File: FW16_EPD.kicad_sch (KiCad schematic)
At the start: 62 parts, among them J1 Conn_01x02, J2 Framework Input Module Connec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, J3 FH34SRJ-24S-0.5SH, J4 FH34SRJ-6S-0.5SH, Q1 DMG3404L, Q2 SSM3J338R, U1 RP2040, U2 W25Q128JVP, U3 MCP9808_DFN, Y1 12.000 MHz ABM8-272-T3

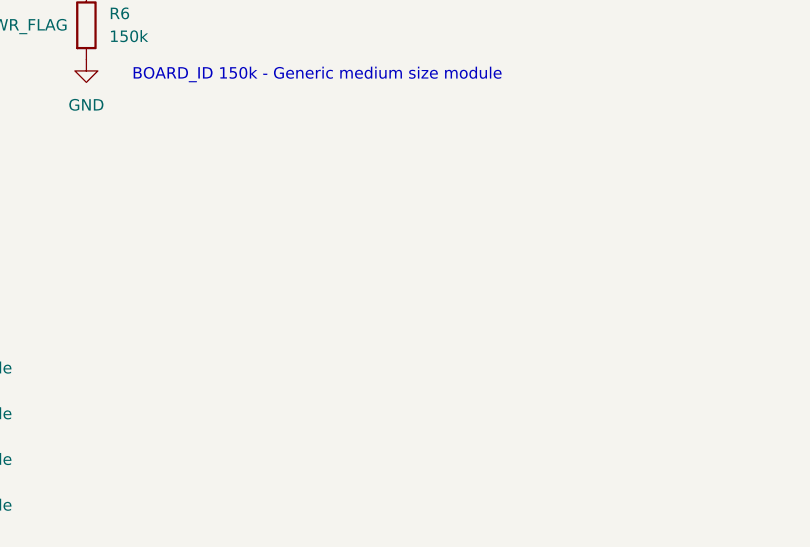
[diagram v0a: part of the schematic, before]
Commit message: sch/pcb: add TVS diodes; thicker traces for EPD DC/DC
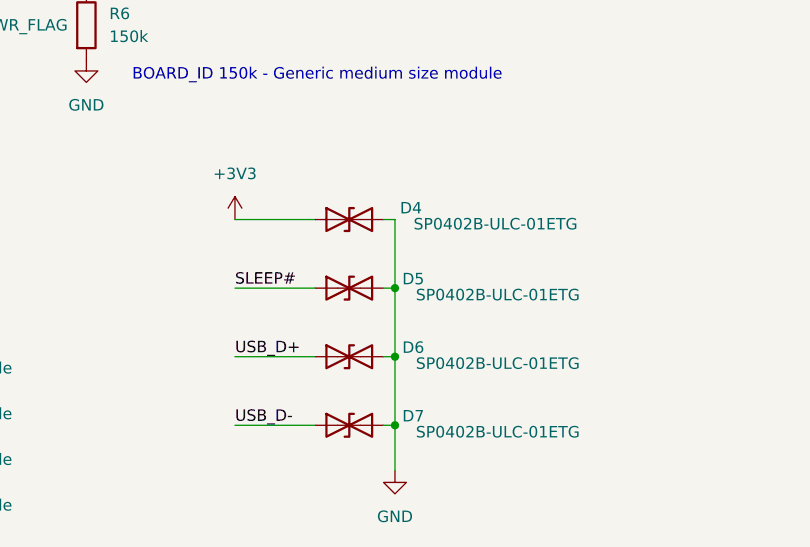
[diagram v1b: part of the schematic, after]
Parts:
- added D4, D5, D6, D7: SP0402B-ULC-01ETG, Diode_SMD:D_0402_1005Metric, symbol Device:D_TVS
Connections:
- net +3V3: now also D4.1 (A1)
- net GND: now also D4.2 (A2), D5.2 (A2), D6.2 (A2), D7.2 (A2)
- net SLEEP#: now also D5.1 (A1)
- net USB_D+: now also D6.1 (A1)
- net USB_D-: now also D7.1 (A1)

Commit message: finishing touches
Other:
- title: (none) -> Framework 16 Touchscreen EPD Module
- moved on the sheet: H1, H2, H3, H4, H5, H6, H7, H8
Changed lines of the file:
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@@
 	(generator_version "8.0")
 	(paper "A3")
+	(title_block
+		(title "Framework 16 Touchscreen EPD Module")
+		(date "2024-10-03")
+		(rev "1.0")
+	)
 	(junction
 		(at 321.31 185.42)
@@
 	(text "Magnet Holes"
 		(exclude_from_sim no)
-		(at 55.118 256.032 0)
+		(at 41.148 261.112 0)
 		(effects
 			(font
@@
 	(text "Alignment Holes"
 		(exclude_from_sim no)
-		(at 25.4 256.286 0)
+		(at 21.59 261.366 0)
 		(effects
 			(font
@@
 	(symbol
 		(lib_id "Mechanical:MountingHole")
-		(at 20.32 260.35 0)
+		(at 16.51 265.43 0)
 		(unit 1)
 		(exclude_from_sim yes)
@@
 		(fields_autoplaced yes)
 		(property "Reference" "H1"
-			(at 22.86 259.0799 0)
+			(at 19.05 264.1599 0)
 			(effects
 				(font
@@
 		)
 		(property "Value" "MountingHole"
-			(at 22.86 261.6199 0)
+			(at 19.05 266.6999 0)
 			(effects
 				(font
@@
 		)
 		(property "Footprint" "MountingHole:MountingHole_2.1mm"
-			(at 20.32 260.35 0)
+			(at 16.51 265.43 0)
 			(effects
 				(font
@@
 		)
 		(property "Datasheet" "~"
-			(at 20.32 260.35 0)
+			(at 16.51 265.43 0)
 			(effects
 				(font
@@
 		)
 		(property "Description" "Mounting Hole without connection"
-			(at 20.32 260.35 0)
+			(at 16.51 265.43 0)
 			(effects
 				(font
@@
 	(symbol
 		(lib_id "Mechanical:MountingHole")
-		(at 50.8 275.59 0)
+		(at 36.83 280.67 0)
 		(unit 1)
 		(exclude_from_sim yes)
@@
 		(fields_autoplaced yes)
 		(property "Reference" "H8"
-			(at 53.34 274.3199 0)
+			(at 39.37 279.3999 0)
 			(effects
 				(font
@@
 		)
 		(property "Value" "MountingHole"
-			(at 53.34 276.8599 0)
+			(at 39.37 281.9399 0)
 			(effects
 				(font
@@
 		)
 		(property "Footprint" "InputModule:MountingHole_3.7mm_Pad_24929"
-			(at 50.8 275.59 0)
+			(at 36.83 280.67 0)
 			(effects
 				(font
@@
 		)
 		(property "Datasheet" "~"
-			(at 50.8 275.59 0)
+			(at 36.83 280.67 0)
 			(effects
 				(font
@@
 		)
 		(property "Description" "Mounting Hole without connection"
-			(at 50.8 275.59 0)
+			(at 36.83 280.67 0)
 			(effects
 				(font
@@
 	(symbol
 		(lib_id "Mechanical:MountingHole")
-		(at 20.32 265.43 0)
+		(at 16.51 270.51 0)
 		(unit 1)
 		(exclude_from_sim yes)
@@
 		(fields_autoplaced yes)
 		(property "Reference" "H2"
-			(at 22.86 264.1599 0)
+			(at 19.05 269.2399 0)
 			(effects
 				(font
@@
 		)
 		(property "Value" "MountingHole"
-			(at 22.86 266.6999 0)
+			(at 19.05 271.7799 0)
 			(effects
 				(font
@@
 		)
 		(property "Footprint" "MountingHole:MountingHole_2.1mm"
-			(at 20.32 265.43 0)
+			(at 16.51 270.51 0)
 			(effects
 				(font
@@
 		)
 		(property "Datasheet" "~"
-			(at 20.32 265.43 0)
+			(at 16.51 270.51 0)
 			(effects
 				(font
@@
 		)
 		(property "Description" "Mounting Hole without connection"
-			(at 20.32 265.43 0)
+			(at 16.51 270.51 0)
 			(effects
 				(font
@@
 	(symbol
 		(lib_id "Mechanical:MountingHole")
-		(at 20.32 275.59 0)
+		(at 16.51 280.67 0)
 		(unit 1)
 		(exclude_from_sim yes)
@@
 		(fields_autoplaced yes)
 		(property "Reference" "H4"
-			(at 22.86 274.3199 0)
+			(at 19.05 279.3999 0)
 			(effects
 				(font
@@
 		)
 		(property "Value" "MountingHole"
-			(at 22.86 276.8599 0)
+			(at 19.05 281.9399 0)
 			(effects
 				(font
@@
 		)
 		(property "Footprint" "MountingHole:MountingHole_2.1mm"
-			(at 20.32 275.59 0)
+			(at 16.51 280.67 0)
 			(effects
 				(font
@@
 		)
 		(property "Datasheet" "~"
-			(at 20.32 275.59 0)
+			(at 16.51 280.67 0)
 			(effects
 				(font
@@
 		)
 		(property "Description" "Mounting Hole without connection"
-			(at 20.32 275.59 0)
+			(at 16.51 280.67 0)
 			(effects
 				(font
@@
 	(symbol
 		(lib_id "Mechanical:MountingHole")
-		(at 50.8 270.51 0)
+		(at 36.83 275.59 0)
 		(unit 1)
 		(exclude_from_sim yes)
@@
 		(fields_autoplaced yes)
 		(property "Reference" "H7"
-			(at 53.34 269.2399 0)
+			(at 39.37 274.3199 0)
 			(effects
 				(font
@@
 		)
 		(property "Value" "MountingHole"
-			(at 53.34 271.7799 0)
+			(at 39.37 276.8599 0)
 			(effects
 				(font
@@
 		)
 		(property "Footprint" "InputModule:MountingHole_3.7mm_Pad_24929"
-			(at 50.8 270.51 0)
+			(at 36.83 275.59 0)
 			(effects
 				(font
@@
 		)
 		(property "Datasheet" "~"
-			(at 50.8 270.51 0)
+			(at 36.83 275.59 0)
 			(effects
 				(font
@@
 		)
 		(property "Description" "Mounting Hole without connection"
-			(at 50.8 270.51 0)
+			(at 36.83 275.59 0)
 			(effects
 				(font
@@
 	(symbol
 		(lib_id "Mechanical:MountingHole")
-		(at 50.8 265.43 0)
+		(at 36.83 270.51 0)
 		(unit 1)
 		(exclude_from_sim yes)
@@
 		(fields_autoplaced yes)
 		(property "Reference" "H6"
-			(at 53.34 264.1599 0)
+			(at 39.37 269.2399 0)
 			(effects
 				(font
@@
 		)
 		(property "Value" "MountingHole"
-			(at 53.34 266.6999 0)
+			(at 39.37 271.7799 0)
 			(effects
 				(font
@@
 		)
 		(property "Footprint" "InputModule:MountingHole_3.7mm_Pad_24929"
-			(at 50.8 265.43 0)
+			(at 36.83 270.51 0)
 			(effects
 				(font
@@
 		)
 		(property "Datasheet" "~"
-			(at 50.8 265.43 0)
+			(at 36.83 270.51 0)
 			(effects
 				(font
@@
 		)
 		(property "Description" "Mounting Hole without connection"
-			(at 50.8 265.43 0)
+			(at 36.83 270.51 0)
 			(effects
 				(font
@@
 	(symbol
 		(lib_id "Mechanical:MountingHole")
-		(at 20.32 270.51 0)
+		(at 16.51 275.59 0)
 		(unit 1)
 		(exclude_from_sim yes)
@@
 		(fields_autoplaced yes)
 		(property "Reference" "H3"
-			(at 22.86 269.2399 0)
+			(at 19.05 274.3199 0)
 			(effects
 				(font
@@
 		)
 		(property "Value" "MountingHole"
-			(at 22.86 271.7799 0)
+			(at 19.05 276.8599 0)
 			(effects
 				(font
@@
 		)
 		(property "Footprint" "MountingHole:MountingHole_2.1mm"
-			(at 20.32 270.51 0)
+			(at 16.51 275.59 0)
 			(effects
 				(font
@@
 		)
 		(property "Datasheet" "~"
-			(at 20.32 270.51 0)
+			(at 16.51 275.59 0)
 			(effects
 				(font
@@
 		)
 		(property "Description" "Mounting Hole without connection"
-			(at 20.32 270.51 0)
+			(at 16.51 275.59 0)
 			(effects
 				(font
@@
 	(symbol
 		(lib_id "Mechanical:MountingHole")
-		(at 50.8 260.35 0)
+		(at 36.83 265.43 0)
 		(unit 1)
 		(exclude_from_sim yes)
@@
 		(fields_autoplaced yes)
 		(property "Reference" "H5"
-			(at 53.34 259.0799 0)
+			(at 39.37 264.1599 0)
 			(effects
 				(font
@@
 		)
 		(property "Value" "MountingHole"
-			(at 53.34 261.6199 0)
+			(at 39.37 266.6999 0)
 			(effects
 				(font
@@
 		)
 		(property "Footprint" "InputModule:MountingHole_3.7mm_Pad_24929"
-			(at 50.8 260.35 0)
+			(at 36.83 265.43 0)
 			(effects
 				(font
@@
 		)
 		(property "Datasheet" "~"
-			(at 50.8 260.35 0)
+			(at 36.83 265.43 0)
 			(effects
 				(font
@@
 		)
 		(property "Description" "Mounting Hole without connection"
-			(at 50.8 260.35 0)
+			(at 36.83 265.43 0)
 			(effects
 				(font
